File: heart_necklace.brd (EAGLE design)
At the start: 33.9 x 31.6 mm, 23 parts, among them SW1 300mA/4V

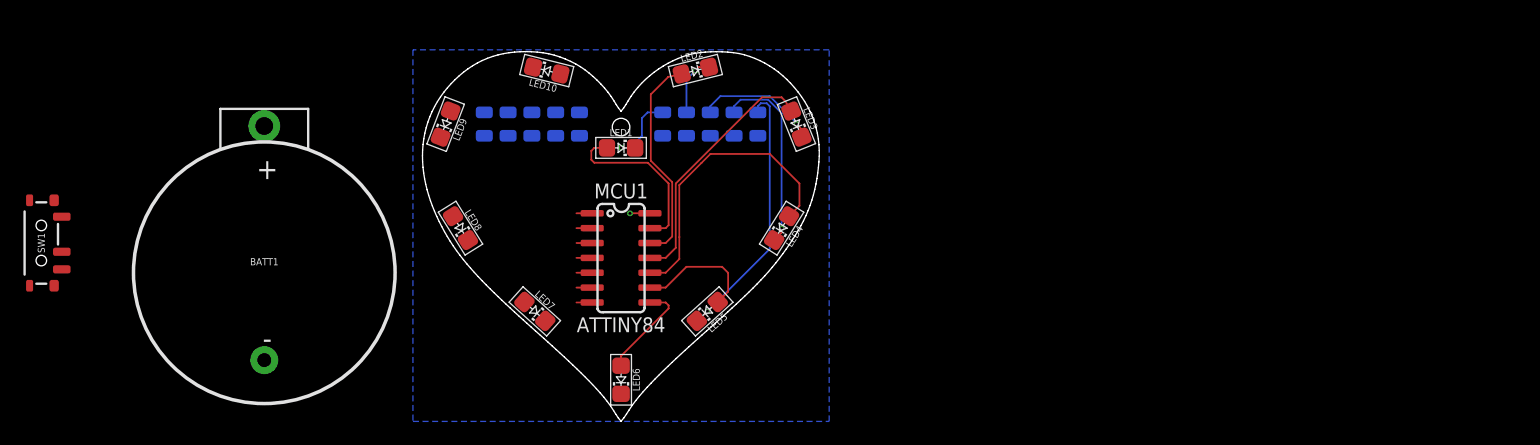
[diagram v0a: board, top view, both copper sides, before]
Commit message: Renamed files to heart_necklace.  Added gitignore.  Did most of routing
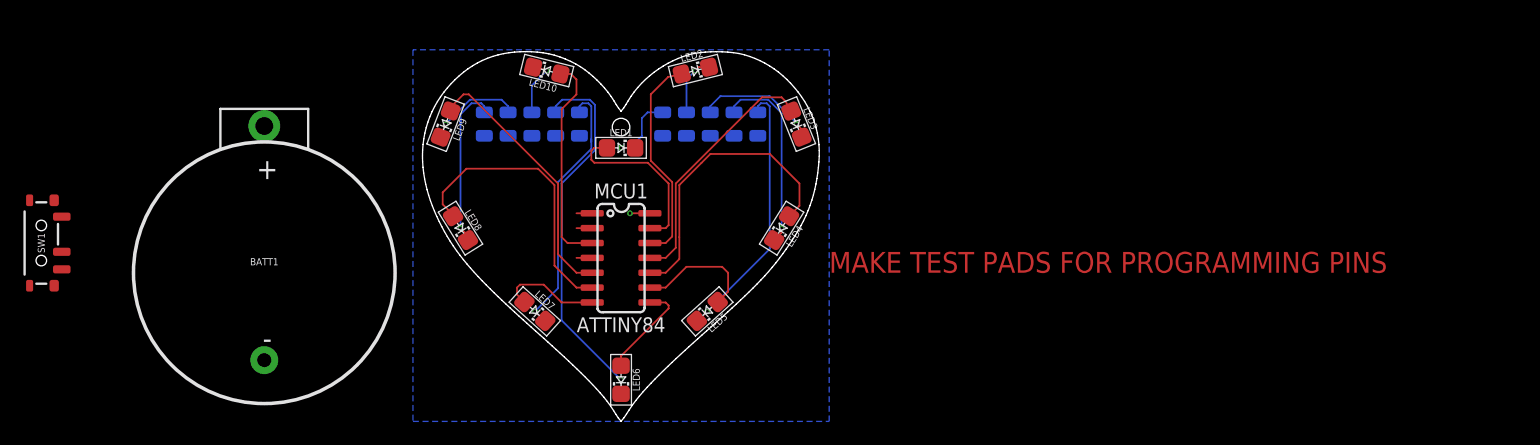
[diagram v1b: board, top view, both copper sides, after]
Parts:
- moved R10 4.06 mm to (-7.62, 25.4)
- moved R8 4.06 mm to (-11.7, 25.4)
- moved R6 2.03 mm to (-5.59, 25.4)
- moved R7 2.03 mm to (-3.56, 25.4)
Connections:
- net LED1: now also LED9.A; no longer LED10.A
- net LED8: now also LED10.A; no longer LED9.A
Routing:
- net N$6: track 0.00 -> 32.3 mm, vias 0 -> 1
- net LED9: track 1.35 -> 24.3 mm
- net N$7: track 0.00 -> 22.8 mm, vias 0 -> 1
- net LED1: track 1.35 -> 22.7 mm
- net LED8: track 1.35 -> 18.4 mm
- net N$8: track 0.00 -> 14.6 mm, vias 0 -> 1
- net N$10: track 0.00 -> 8.17 mm, vias 0 -> 1
- net LED10: track 1.35 -> 8.65 mm
- net N$9: track 0.00 -> 4.90 mm, vias 0 -> 1
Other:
- board text added: "MAKE TEST PADS FOR PROGRAMMING PINS"

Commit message: Almost done with heart necklace
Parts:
- removed BATT1: 3V/CR2032, PiB:BATTERY_COINCELL-20MM-PTH
- added AVR_ISP1: (no value), PiB_connectors:2X3-NS-PAD
- added BATT2: BR-1225/3V/48mAh, PiB_batteries:BR-1225
- moved SW1 46.9 mm to (-3.43, 6.48), flipped to the bottom, turned to 133 degrees
- moved R1 7.27 mm to (10.2, 28.4), turned to 180 degrees
- moved R7 7.27 mm to (-10.2, 22.4), turned to 0 degrees
- moved R6 6.83 mm to (-10.2, 20.3), turned to 0 degrees
- moved R5 5.18 mm to (10.2, 20.4), turned to 180 degrees
- moved R2 4.68 mm to (10.2, 26.4), turned to 180 degrees
- moved R10 3.97 mm to (-10.2, 28.4), turned to 0 degrees
- moved R4 2.96 mm to (10.2, 22.5), turned to 180 degrees
- moved R3 2.69 mm to (10.2, 24.5), turned to 180 degrees
- moved R8 1.83 mm to (-10.2, 24.4), turned to 0 degrees
- moved R9 1.14 mm to (-10.2, 26.4), turned to 0 degrees
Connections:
- removed net N$14: MCU1.4
- new net !RESET: AVR_ISP1.5, MCU1.4
- new net VCC: AVR_ISP1.2
- net GND: now also AVR_ISP1.6, BATT2.-; no longer BATT1.-
- net LED10: now also AVR_ISP1.4
- net LED4: now also AVR_ISP1.1
- net LED6: now also AVR_ISP1.3
- net VBATT: now also BATT2.+_1, BATT2.+_2; no longer BATT1.+
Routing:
- net VBATT: track 0.00 -> 25.3 mm, vias 0 -> 2
- net N$1: track 6.90 -> 17.2 mm
- net N$11: track 1.35 -> 11.6 mm, vias 0 -> 1
- net N$5: track 22.7 -> 14.9 mm
- net N$4: track 16.4 -> 8.69 mm
- net GND: track 1.70 -> 8.07 mm
- net N$2: track 5.17 -> 11.2 mm
- net N$7: track 22.8 -> 17.0 mm
- net N$3: track 10.6 -> 5.49 mm
- net N$8: track 14.6 -> 10.6 mm
- net N$9: track 4.90 -> 8.17 mm
- net N$10: track 8.17 -> 5.46 mm
- net N$17: track 1.35 -> 0.00 mm
- net N$14: track 1.35 -> 0.00 mm
- net N$6: track 32.3 -> 31.5 mm

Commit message: Rev 1: Heart Necklace complete
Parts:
- removed AVR_ISP1: (no value), PiB_connectors:2X3-NS-PAD
- LED1, LED10, LED2, LED3, LED4, LED5, LED6, LED7, LED8, LED9: device PiB_leds:LED_SMD-805_ -> PiB_leds:LED_SMD-805_NO-SILK
- MCU1: device PiB_ic_microcontrollers:SO-14 -> PiB_ic_microcontrollers:SO-14_NO-SILK
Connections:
- removed net VCC: AVR_ISP1.2
- net !RESET: no longer AVR_ISP1.5
- net GND: no longer AVR_ISP1.6
- net LED10: no longer AVR_ISP1.4
- net LED4: no longer AVR_ISP1.1
- net LED6: no longer AVR_ISP1.3
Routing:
- net LED10: track 8.65 -> 10.4 mm
- net LED8: track 18.4 -> 17.3 mm
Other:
- board text added: "Designed by: MrSwirlyEyes"
- board text added: "Heart Necklace"
- board text added: "Rev 1"
- board text added: "Techteia"
- board text removed: "MAKE TEST PADS FOR PROGRAMMING PINS"

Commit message: changes
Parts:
- removed BATT2: BR-1225/3V/48mAh, PiB_batteries:BR-1225
- added BATT1: (no value), PiB_batteries:CR-2032
- added C1, C2: 10uF/10V, PiB_capacitors:_CER_SMD_0402
- MCU1: value ATTINY84 -> ATTiny84
- moved SW1 20.2 mm to (-15.6, 22.6), turned to 171 degrees
- moved R6 10.7 mm to (-4.95, 29.7), turned to 270 degrees
- moved R5 9.84 mm to (6.86, 29.7), turned to 270 degrees
- moved R7 8.07 mm to (-6.86, 29.7), turned to 270 degrees
- moved R4 7.37 mm to (8.76, 29.7), turned to 270 degrees
- moved R8 5.51 mm to (-8.76, 29.7), turned to 270 degrees
- moved R1 5.36 mm to (4.95, 29.7), turned to 270 degrees
- moved R3 5.23 mm to (10.7, 29.7), turned to 270 degrees
- moved R2 4.09 mm to (12.6, 29.7), turned to 270 degrees
- moved R9 3.34 mm to (-10.7, 29.7), turned to 270 degrees
- moved MCU1 3.17 mm to (0.00, 17.1)
- moved R10 2.73 mm to (-12.6, 29.7), turned to 270 degrees
- moved LED3 2.40 mm to (16.3, 27.4)
- moved LED9 2.40 mm to (-16.3, 27.4)
- moved LED10 2.30 mm to (-6.60, 32.3)
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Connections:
- net GND: now also BATT1.-, C1.2, C2.2; no longer BATT2.-
- net N$11: now also C1.1, C2.1, SW1.3; no longer SW1.2
- net VBATT: now also BATT1.+_1, BATT1.+_2, SW1.2; no longer BATT2.+_1, BATT2.+_2, SW1.1
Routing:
- net N$7: track 17.0 -> 45.9 mm
- net VBATT: track 25.3 -> 47.4 mm
- net N$11: track 11.6 -> 30.1 mm
- net N$5: track 14.9 -> 30.1 mm
- net N$8: track 10.6 -> 20.9 mm
- net N$1: track 17.2 -> 8.06 mm
- net N$4: track 8.69 -> 17.8 mm
- net N$6: track 31.5 -> 40.2 mm
- net GND: track 8.07 -> 1.45 mm
- net LED2: track 14.9 -> 8.56 mm
- net N$9: track 8.65 -> 13.7 mm
- net LED4: track 8.54 -> 11.8 mm
- net LED1: track 22.7 -> 25.9 mm
- net LED5: track 24.9 -> 21.8 mm
- net LED3: track 21.6 -> 24.7 mm
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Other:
- board size 33.9 x 31.6 mm -> 36.5 x 34 mm
- board text added: "Rev 2"
- board text removed: "Rev 1"
